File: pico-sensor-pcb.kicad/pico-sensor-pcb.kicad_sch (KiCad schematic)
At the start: 8 parts, among them J10 Conn_PCB_2, J11 Conn_I2C1, J13 Conn_I2C1, J7 Conn_PCB_1

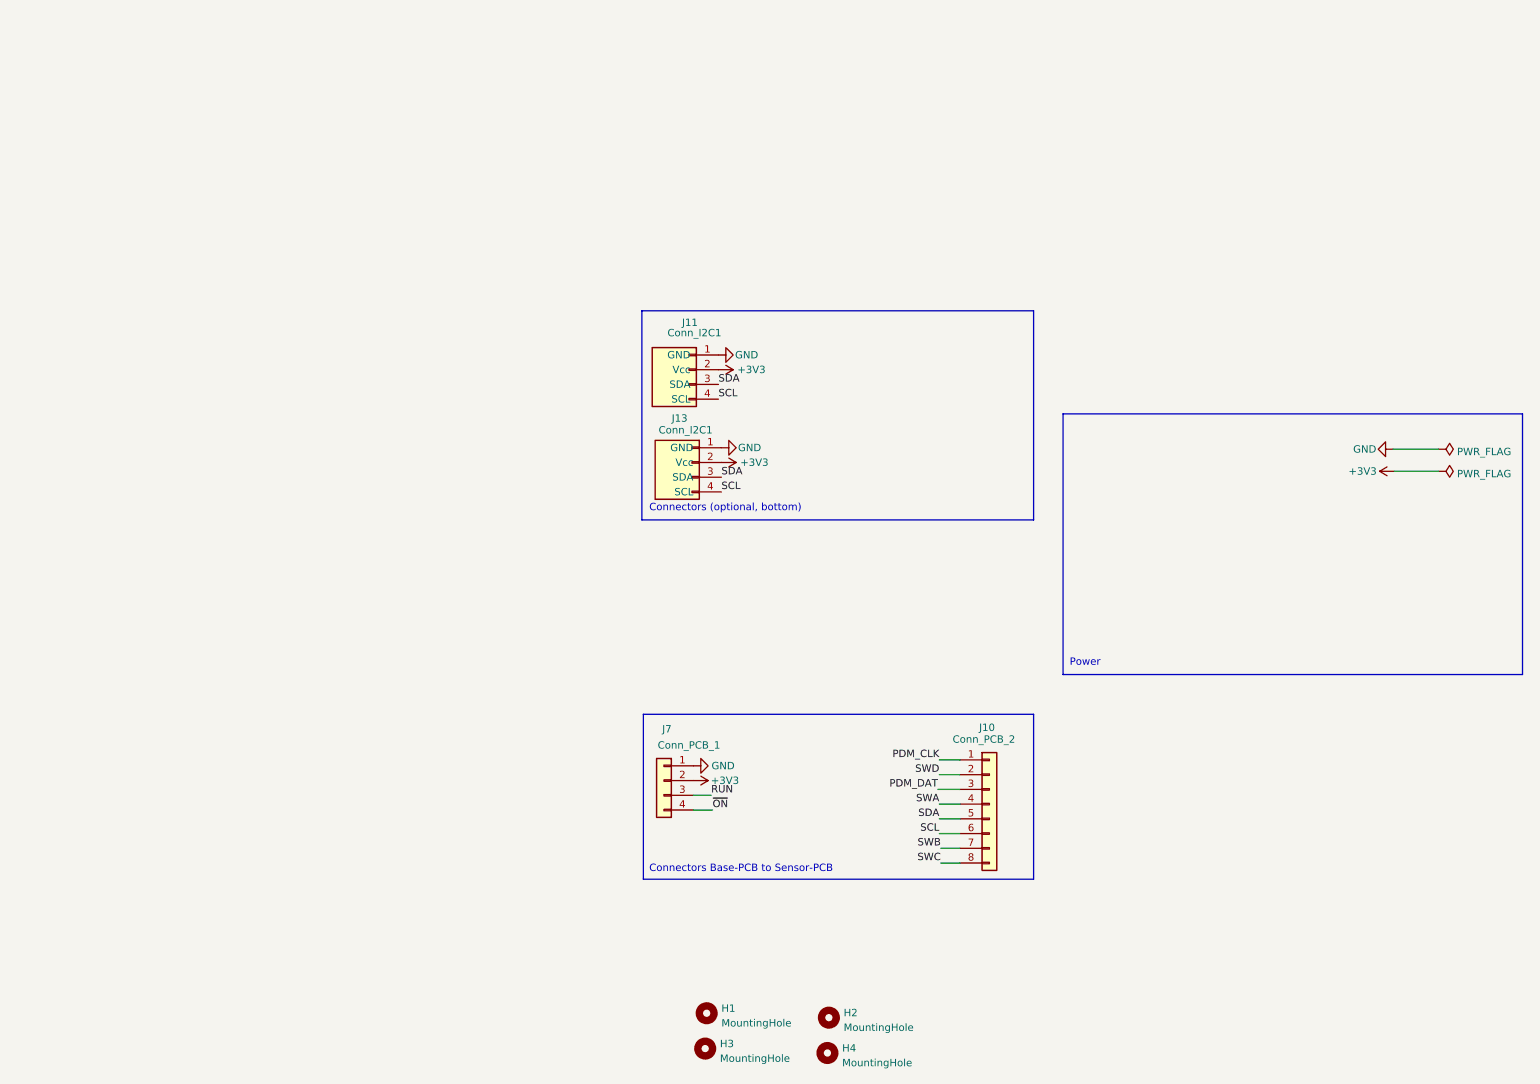
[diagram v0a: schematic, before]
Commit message: added basic components, implement AHT20 and BH1750
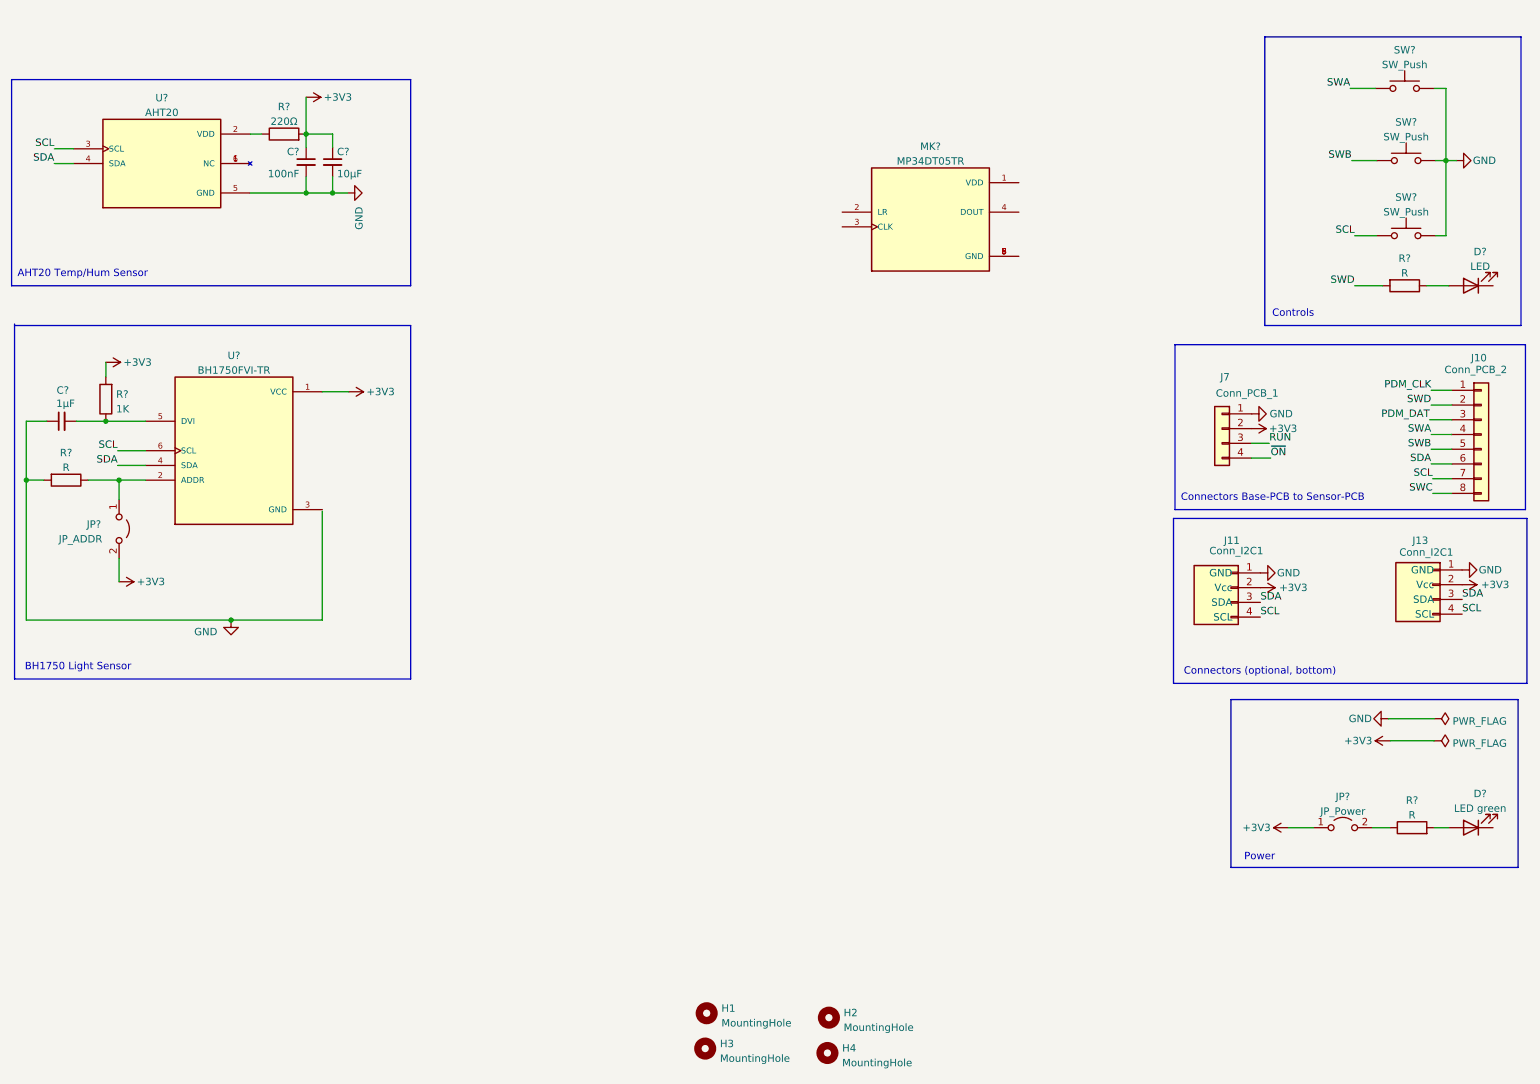
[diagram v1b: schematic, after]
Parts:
- added C?: 10µF, symbol Device:C_Small
- added C?: 100nF, symbol Device:C_Small
- added C?: 1µF, symbol Device:C_Small
- added D?: LED green, symbol Device:LED
- added D?: LED, symbol Device:LED
- added JP?: JP_ADDR, symbol Jumper:Jumper_2_Open
- added JP?: JP_Power, symbol Jumper:Jumper_2_Open
- added MK?: MP34DT05TR, MP34DT05TR:MIC_MP34DT05TR, symbol user:MP34DT05TR
- added R? (x3): R, symbol Device:R
- added R?: 1K, symbol Device:R
- added R?: 220Ω, symbol Device:R
- added SW? (x3): SW_Push, symbol Switch:SW_Push
- added U?: AHT20, AHT20:PSON100P300X300X110-6N, symbol user:AHT20
- added U?: BH1750FVI-TR, BH1750FVI-TR:XDCR_BH1750FVI-TR, symbol user:BH1750FVI-TR
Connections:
- net +3V3: now also C?.1, C?.1, JP?.1 (A), JP?.2 (B), R?.2, R?.2, U?.1 (VCC)
- net GND: now also C?.1, C?.2, C?.2, R?.2, SW?.2, SW?.2, SW?.2, U?.5 (GND)
- net SCL: now also J10.7 (Pin_7), SW?.1, U?.3 (SCL), U?.6 (SCL); no longer J10.6 (Pin_6)
- net SDA: now also J10.6 (Pin_6), U?.4 (SDA), U?.4 (SDA); no longer J10.5 (Pin_5)
- net SWA: now also SW?.1
- net SWB: now also J10.5 (Pin_5), SW?.1; no longer J10.7 (Pin_7)
- net SWD: now also R?.2
- new net: D?.2 (A), R?.2
- new net: JP?.1 (A), R?.1, U?.2 (ADDR)
- new net: MK?.5 (GND), MK?.6 (GND), MK?.7 (GND), MK?.8 (GND)
- new net: D?.2 (A), R?.1
- new net: U?.1 (NC), U?.6 (NC)
- new net: R?.1, U?.2 (VDD)
- new net: JP?.2 (B), R?.1
- new net: C?.2, R?.1, U?.5 (DVI)
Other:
- note added: "AHT20 Temp/Hum Sensor"
- note added: "BH1750 Light Sensor"
- note added: "Controls"
- moved on the sheet: J10, J11, J13, J7

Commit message: basic schematic with AHT20, BH1750, PDM-mic, buttons, LEDs (incl. footprints/components)
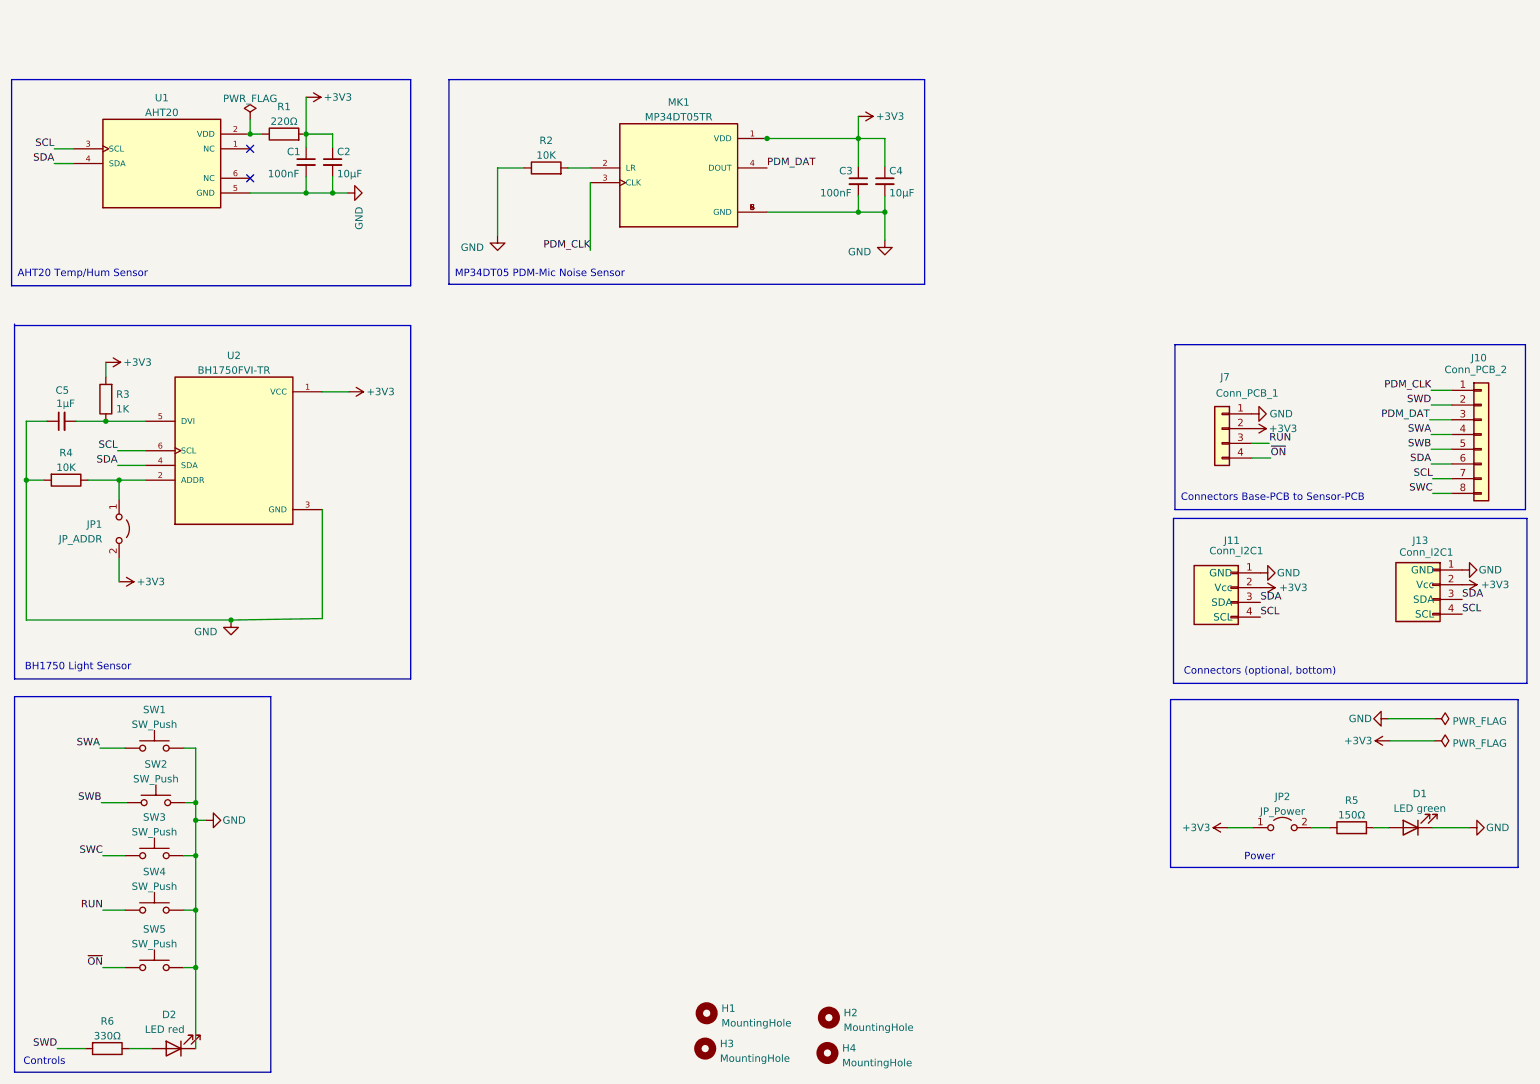
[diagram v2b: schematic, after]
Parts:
- added C3: 100nF, Capacitor_SMD:C_0402_1005Metric, symbol Device:C_Small
- added C4: 10µF, Capacitor_SMD:C_0603_1608Metric, symbol Device:C_Small
- added R2: 10K, Resistor_SMD:R_0402_1005Metric, symbol Device:R
- added SW4, SW5: SW_Push, Button_Switch_SMD:SW_SPST_B3S-1000, symbol Switch:SW_Push
- C1: renamed from C?; footprint (none) -> Capacitor_SMD:C_0402_1005Metric; LCSC (none) -> C1525
- C2: renamed from C?; footprint (none) -> Capacitor_SMD:C_0603_1608Metric; LCSC (none) -> C19702
- C5: renamed from C?; footprint (none) -> Capacitor_SMD:C_0603_1608Metric; LCSC (none) -> C15849
- D1: renamed from D?; footprint (none) -> LED_SMD:LED_0805_2012Metric; LCSC (none) -> C2297
- D2: renamed from D?; value LED -> LED red; footprint (none) -> LED_SMD:LED_0805_2012Metric; LCSC (none) -> C84256
- J10: footprint Connector_JST:JST_SUR_SM08B-SURS-TF_1x08-1MP_P0.80mm_Horizontal -> Connector_JST:JST_SUR_BM08B-SURS-TF_1x08-1MP_P0.80mm_Vertical; LCSC (none) -> C5143489
- J11: LCSC (none) -> C160404
- J7: footprint Connector_JST:JST_SUR_SM04B-SURS-TF_1x04-1MP_P0.80mm_Horizontal -> Connector_JST:JST_SUR_BM04B-SURS-TF_1x04-1MP_P0.80mm_Vertical; LCSC (none) -> C495551
- JP1, JP2: renamed from JP?; footprint (none) -> Jumper:SolderJumper-2_P1.3mm_Open_Pad1.0x1.5mm
- MK1: renamed from MK?; LCSC (none) -> C2688664
- R1: renamed from R?; footprint (none) -> Resistor_SMD:R_0402_1005Metric; LCSC (none) -> C22962
- R3: renamed from R?; footprint (none) -> Resistor_SMD:R_0402_1005Metric; LCSC (none) -> C11702
- R4: renamed from R?; value R -> 10K; footprint (none) -> Resistor_SMD:R_0402_1005Metric; LCSC (none) -> C25744
- R5: renamed from R?; value R -> 150Ω; footprint (none) -> Resistor_SMD:R_0402_1005Metric; LCSC (none) -> C25082
- R6: renamed from R?; value R -> 330Ω; footprint (none) -> Resistor_SMD:R_0402_1005Metric; LCSC (none) -> C25104
- SW1, SW2, SW3: renamed from SW?; footprint (none) -> Button_Switch_SMD:SW_SPST_B3S-1000; LCSC (none) -> C221869
- U1: renamed from U?; LCSC (none) -> C2757850
- gave numbers to parts that had none: 1
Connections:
- net +3V3: now also MK1.1 (VDD), C3.1, C4.1
- net GND: now also D1.1 (K), D2.1 (K), MK1.5 (GND), MK1.6 (GND), MK1.7 (GND), MK1.8 (GND), U2.3 (GND), C3.2, C4.2, R2.1, SW4.2, SW5.2
- net PDM_CLK: now also MK1.3 (CLK)
- net PDM_DAT: now also MK1.4 (DOUT)
- net RUN: now also SW4.1
- net SCL: no longer SW3.1
- net SWC: now also SW3.1
- net ~{ON}: now also SW5.1
- net at MK1.2 (LR): now also R2.2
- net at U1.1 (NC): no longer U1.6 (NC)
- no-connect marks 0 -> 2
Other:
- note added: "MP34DT05 PDM-Mic Noise Sensor"
- moved on the sheet: D1, D2, JP2, MK1, R5, R6, SW1, SW2, SW3

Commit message: (very) initial pcb-layout for sensor-board
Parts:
- J13: footprint Connector_PinHeader_2.54mm:PinHeader_1x04_P2.54mm_Vertical -> Connector_PinHeader_2.54mm:PinHeader_1x04_P2.54mm_Horizontal; now left out of the parts list
- MK1: footprint MP34DT05TR:MIC_MP34DT05TR -> user:MP34DT05TR; Availability In Stock -> (none); Check_prices https://www.snapeda.com/parts/MP34DT05TR/STMicroelectronics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 -> (none); LCSC C2688664 -> (none); MANUFACTURER STMicroelectronics -> (none); MAXIMUM_PACKAGE_HEIGHT 1.1mm -> (none); MF STMicroelectronics -> (none); MP MP34DT05TR -> (none); PARTREV 2 -> (none); Package WLCSP-28 STMicroelectronics -> (none); Price None -> (none); Purchase-URL https://www.snapeda.com/api/url_track_click_mouser/?unipart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 -> (none); STANDARD Manufacturer Recommendation -> (none); SnapEDA_Link https://www.snapeda.com/parts/MP34DT05TR/STMicroelectronics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 -> (none)
- U1: footprint AHT20:PSON100P300X300X110-6N -> user:AHT20; Availability Not in stock -> (none); Check_prices https://www.snapeda.com/parts/AHT20/Asair/view-part/?ref=eda -> (none); LCSC C2757850 -> (none); MANUFACTURER Asair -> (none); MAXIMUM_PACKAGE_HEIGHT 1.1mm -> (none); MF Asair -> (none); PARTREV V1.0 -> (none); Package Package -> (none); Price None -> (none); STANDARD IPC 7351B -> (none); SnapEDA_Link https://www.snapeda.com/parts/AHT20/Asair/view-part/?ref=sn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 -> (none)
- U2: footprint BH1750FVI-TR:XDCR_BH1750FVI-TR -> user:BH1750; Availability In Stock -> (none); Check_prices https://www.snapeda.com/parts/BH1750FVI-TR/Rohm/view-part/?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 -> (none); LCSC C78960 -> (none); MANUFACTURER Rohm -> (none); MAXIMUM_PACKAGE_HEIGHT 0.75mm -> (none); MF Rohm -> (none); MP BH1750FVI-TR -> (none); PARTREV D -> (none); Package SMD-6 ROHM Semiconductor -> (none); Price None -> (none); Purchase-URL https://www.snapeda.com/api/url_track_click_mouser/?unipart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 -> (none); STANDARD Manufacturer recommendations -> (none); SnapEDA_Link https://www.snapeda.com/parts/BH1750FVI-TR/Rohm/view-part/?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 -> (none)
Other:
- note added: "Notes: - add bottom connector for PDM - add THT for ENS160 - add symbol images for on/rst/mic/temp/lux"

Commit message: Rev 0.7: ready for review
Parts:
- added C6: 100nF, Capacitor_SMD:C_0402_1005Metric, symbol Device:C_Small
- added J1: Conn_PDM, Connector_PinHeader_2.54mm:PinHeader_1x04_P2.54mm_Vertical, symbol Connector_Generic:Conn_01x04
- added J2: Conn_RUN_ON, Connector_PinHeader_2.54mm:PinHeader_1x02_P2.54mm_Vertical, symbol Connector_Generic:Conn_01x02
- added U3: SCD40_Breakout, user:SCD40_Breakout, symbol user:SCD40_Breakout
- added U4: ENS160_Breakout, user:ENS160_Breakout, symbol user:ENS160_Breakout
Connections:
- net +3V3: now also C6.1, J1.3 (Pin_3), U3.2 (VDD), U4.8 (3V3); no longer C1.1, C2.1
- net GND: now also C6.2, J1.4 (Pin_4), U3.1 (GND), U4.9 (GND)
- net PDM_CLK: now also J1.1 (Pin_1)
- net PDM_DAT: now also J1.2 (Pin_2)
- net RUN: now also J2.1 (Pin_1)
- net SCL: now also U3.3 (SCL), U4.10 (SCL)
- net SDA: now also U3.4 (SDA), U4.11 (SDA)
- net ~{ON}: now also J2.2 (Pin_2)
- net at R1.1, U1.2 (VDD): now also C1.1, C2.1
- no-connect marks 2 -> 9
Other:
- note added: "Optional Breakouts"
- note removed: "Notes: - add bottom connector for PDM - add THT for ENS160 - add symbol images for on/rst/mic/temp/lux"
- moved on the sheet: J10, J7, R1
